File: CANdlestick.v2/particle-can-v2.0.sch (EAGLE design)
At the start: 11 parts, among them IC1 LM2940, IC2 TJA1049, J1 OBDII

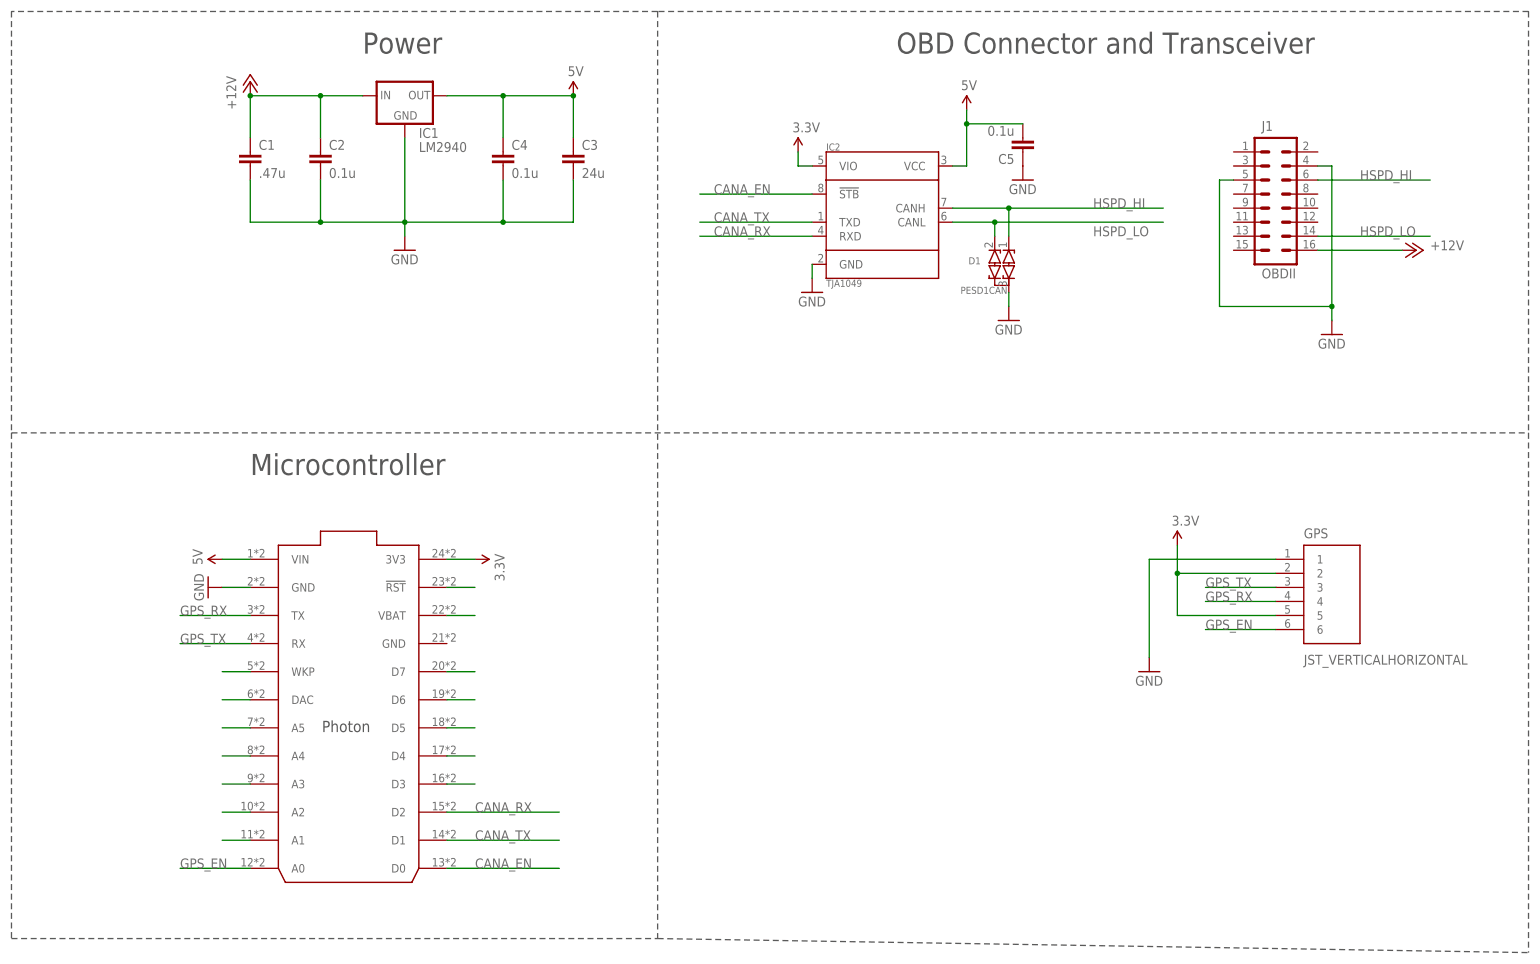
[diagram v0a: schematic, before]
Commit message: Version 2 of the PCB has optimized components and GPS
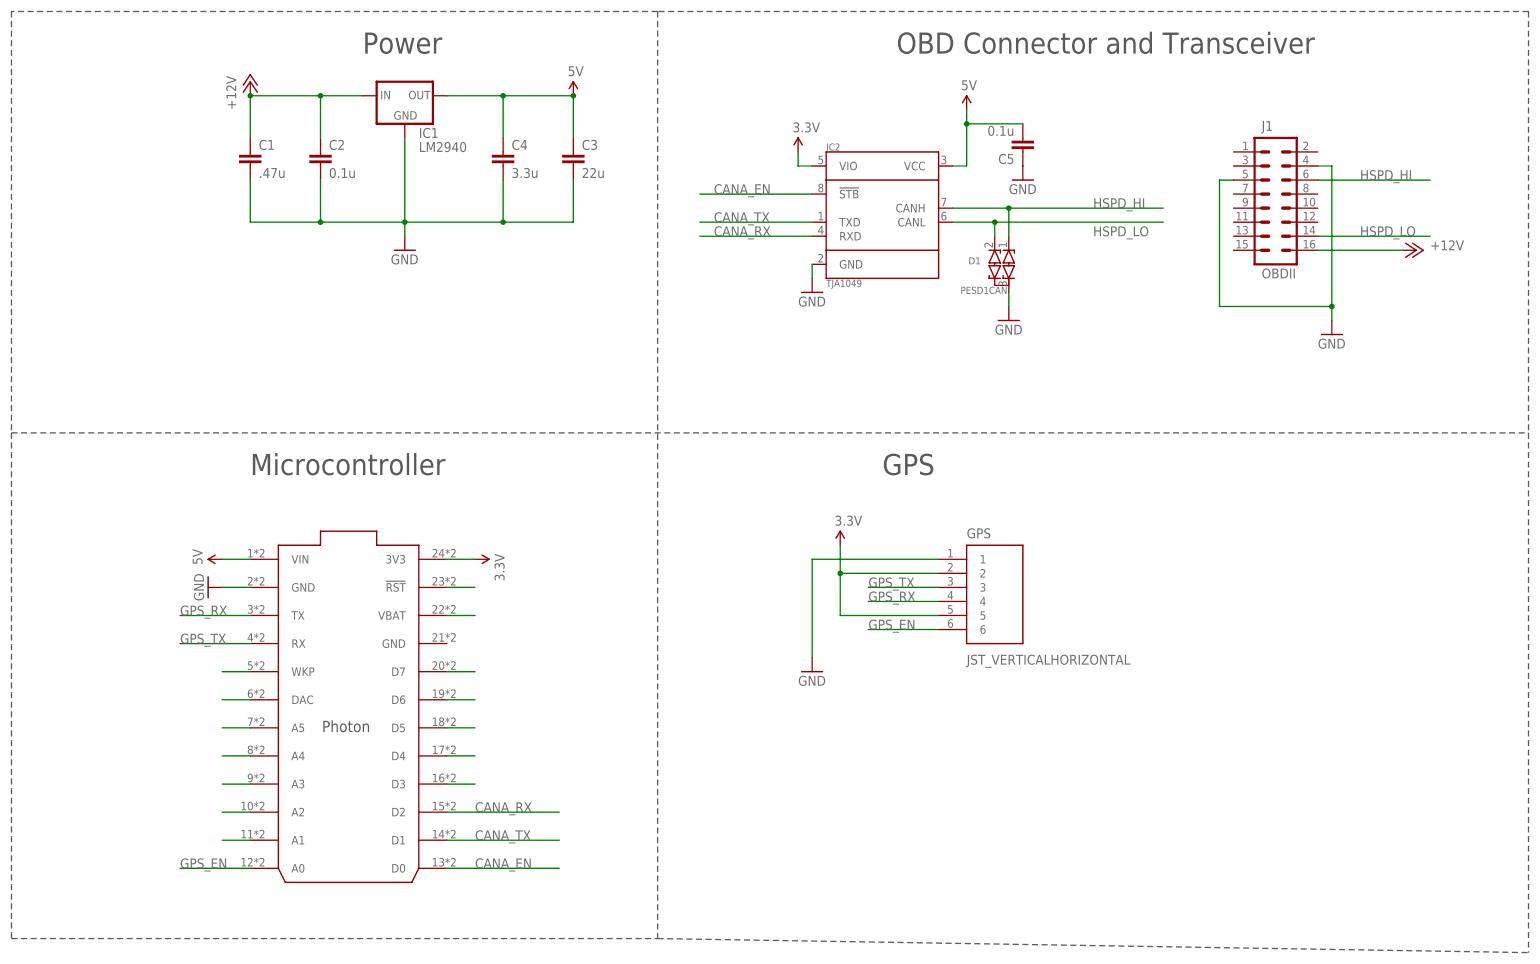
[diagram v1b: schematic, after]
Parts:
- C1: PARTNO 06035A101JAT2A -> C0805C474K5RACTU
- C2: PARTNO 06035A101JAT2A -> 08055C104KAT2A
- C3: value 24u -> 22u; PARTNO CC0805KKX7R9BB474 -> GRM219R61A226MEA0D
- C4: value 0.1u -> 3.3u; PARTNO CC0805KKX7R9BB474 -> C0805C335K8PACTU
- C5: PARTNO CC0603JRX7R7BB104 -> 08055C104KAT2A
- CORE: device Particle:PHOTONWITH_EXTERNAL_HEADERS -> MuniRent:PHOTONWITH_EXTERNAL_HEADERS
- D1: device BUG:DIODE_ESD_DUAL-SOT-23 -> MuniRent:DIODE_ESD_DUAL-SOT-23; PARTNO PESD1CAN,215 -> PESD1CAN-215
- GPS: device SparkFun-Connectors:JST_VERTICALHORIZONTAL -> MuniRent:JST_VERTICALHORIZONTAL; PARTNO (none) -> JST-6-HOR
- IC1: device BUG:LM2940 -> MuniRent:LM2940; PARTNO (none) -> LM2940IMP-5.0/NOPB
- IC2: device BUG:TJA1049 -> MuniRent:TJA1049; PARTNO (none) -> TJA1049T-118
- J1: device BUG:M08X2STRAIGHT -> MuniRent:M08X2STRAIGHT
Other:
- note added: "GPS"
- moved on the sheet: GPS
